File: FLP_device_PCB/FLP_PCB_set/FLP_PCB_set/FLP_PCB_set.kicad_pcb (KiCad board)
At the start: 2 copper layers, 157.8 x 70 mm, 81 parts, among them J3 GRPB052VWVN-RC, J4 OLED, J5 SMA-J-P-X-ST-TH1, Q1 Q_PMOS_DSG, Q2 UMH3N, U1 ESP32-WROOM-32E, U2 TPS61200DRC, U3 MCP73831-2-OT, U4 AMS1117-3.3, U5 CP2104, U6 L86-M33, U7 SX1278, U8 USBLC6-2P6, Y1 32MHz

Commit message: FLP_set add
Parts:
- removed F1: 0603L100SLYR, Resistor_SMD:R_0603_1608Metric
- removed FL1: BLM21PG221SN1D, BLM21PG221SN1D:BEADC2012X105N
- removed R20, R32, R33: 10K, Resistor_SMD:R_0603_1608Metric
- removed R21: 5.1K, Resistor_SMD:R_0402_1005Metric
- removed R30: 22R, Resistor_SMD:R_0402_1005Metric
- removed R31: 1K, Resistor_SMD:R_0603_1608Metric
- removed UART1: 12402012E212A, 12402012E212A:AMPHENOL_12402012E212A
- added BZ1: Buzzer, Buzzer_Beeper:Buzzer_12x9.5RM7.6, F.Cu at (178.4, 110.1)
- added C1: 1uF, Capacitor_SMD:C_0603_1608Metric, F.Cu at (70.7, 155.2)
- added C2: 0.1uF, Capacitor_SMD:C_0603_1608Metric, F.Cu at (66.7, 165.3)
- added C26: 22uF, Capacitor_SMD:C_0805_2012Metric, F.Cu at (172.3, 149.6)
- added C3: PESD0402-140, PESD0402-140:RESC1005X35N, F.Cu at (89.5, 155.0)
- added C36: 0.1uF, Capacitor_SMD:C_0603_1608Metric, F.Cu at (166.1, 104.6)
- added C38: 20pF, Capacitor_SMD:C_0402_1005Metric, F.Cu at (165.5, 124.4)
- added C39: 20pF, Capacitor_SMD:C_0402_1005Metric, F.Cu at (165.5, 126.4)
- added C40: 18pF, Capacitor_SMD:C_0603_1608Metric, F.Cu at (166.1, 109.6)
- added C41: 18pF, Capacitor_SMD:C_0603_1608Metric, F.Cu at (166.1, 112.1)
- added C42: 22uF, Capacitor_SMD:C_0805_2012Metric, F.Cu at (159.0, 142.4)
- added D2: BAT ON, LED_SMD:LED_0805_2012Metric, F.Cu at (94.1, 125.4)
- added D3: TEST, LED_SMD:LED_0805_2012Metric, F.Cu at (94.1, 128.4)
- added D4: USB_ON, LED_SMD:LED_0805_2012Metric, F.Cu at (94.1, 122.4)
- added D5: MBR120VLSFT1G, MBR120VLSFT1G:DIOM3616X98N, F.Cu at (178.1, 151.3)
- added D6: BAT ON, LED_SMD:LED_0805_2012Metric, F.Cu at (176.7, 154.4)
- added D7: USB_ON, LED_SMD:LED_0805_2012Metric, F.Cu at (179.7, 132.9)
- added Find_Host2: SKRPABE010, Diode_SMD:SW_SKRPABE010, F.Cu at (172.0, 105.7)
- added ID1: SKRPABE010, Diode_SMD:SW_SKRPABE010, F.Cu at (172.0, 110.5)
- added J1: GRPB052VWVN-RC, Varistor:SULLINS_GRPB052VWVN-RC, F.Cu at (91.2, 141.6)
- added J10: 61300311121, 61300311121:WURTH_61300311121, F.Cu at (161.9, 152.5)
- added J2: OLED, HTSW-104-20-TM-S:SAMTEC_HTSW-104-20-TM-S, F.Cu at (70.5, 171.0)
- added J6: USB_C_Receptacle_USB2.0_16P, 12402012E212A:AMPHENOL_12402012E212A, F.Cu at (162.4, 137.5)
- added J7: B2B-PH-K-S, B2B_PH_K_S:JST_B2B-PH-K-S, F.Cu at (173.8, 134.4)
- added J8: SMA-J-P-X-ST-TH1, SMA-J-P-X-ST-TH1:SAMTEC_SMA-J-P-X-ST-TH1, F.Cu at (146.4, 135.9)
- added J9: 61300311121, 61300311121:WURTH_61300311121, F.Cu at (161.9, 148.4)
- added L2: 18nH, Capacitor_SMD:C_0402_1005Metric, F.Cu at (92.4, 162.8)
- added L3: 47nH, Capacitor_SMD:C_0402_1005Metric, F.Cu at (140.5, 140.3)
- added R17: 5.1K, Resistor_SMD:R_0402_1005Metric, F.Cu at (96.5, 149.1)
- added R18: 10K, Resistor_SMD:R_0603_1608Metric, F.Cu at (74.7, 162.7)
- added R19: 10K, Resistor_SMD:R_0603_1608Metric, F.Cu at (74.7, 160.2)
- added R24: 2K, Resistor_SMD:R_0402_1005Metric, F.Cu at (176.7, 142.1)
- added R26: 10K, Resistor_SMD:R_0603_1608Metric, F.Cu at (166.1, 114.6)
- added R27: 1M, Resistor_SMD:R_0603_1608Metric, F.Cu at (166.1, 117.2)
- added R28: 10K, Resistor_SMD:R_0603_1608Metric, F.Cu at (166.1, 119.7)
- added S2: SKRPABE010, Diode_SMD:SW_SKRPABE010, F.Cu at (172.0, 115.2)
- added U10: AP2112K-3.3, Package_TO_SOT_SMD:SOT-23-5, F.Cu at (177.1, 147.5)
- added U11: MCP73831-2-OT, Package_TO_SOT_SMD:SOT-23-5, F.Cu at (172.6, 140.5)
- added U12: L86-M33, L86-M33:XCVR_L86-M33, F.Cu at (150.6, 115.4)
- added U13: SX1278, Package_DFN_QFN:QFN-28-1EP_6x6mm_P0.65mm_EP4.8x4.8mm, F.Cu at (146.1, 144.6)
- added U14: CH340N, Package_SO:SOP-8_3.9x4.9mm_P1.27mm, F.Cu at (143.3, 154.1)
- added U9: STM32F103C8T6, STM32F103C8T6:QFP50P900X900X160-48N, F.Cu at (182.1, 122.6)
- added Y2: 32MHz, Crystal:Crystal_SMD_2016-4Pin_2.0x1.6mm, F.Cu at (152.9, 133.2)
- added Y3: ABM3B-8.000MHZ-B2-T, ABM3B-8.000MHZ-B2-T:XTAL_ABM3B-8.000MHZ-B2-T, F.Cu at (171.3, 121.3)
- added Y4: 32.768kHz, Crystal:Crystal_SMD_3215-2Pin_3.2x1.5mm, F.Cu at (170.6, 126.6)
- C10, C9: value 4.7uF -> 22uF; footprint Capacitor_SMD:C_0603_1608Metric -> Capacitor_SMD:C_0805_2012Metric
- C11, C6: value 22uF -> PESD0402-140; footprint Capacitor_SMD:C_0805_2012Metric -> PESD0402-140:RESC1005X35N
- C12, C33: value 22uF -> 0.1uF; footprint Capacitor_SMD:C_0805_2012Metric -> Capacitor_SMD:C_0603_1608Metric
- C13: value PESD0402-140 -> 4.7uF; footprint PESD0402-140:RESC1005X35N -> Capacitor_SMD:C_0603_1608Metric
- C14, C16: value PESD0402-140 -> 22uF; footprint PESD0402-140:RESC1005X35N -> Capacitor_SMD:C_0805_2012Metric
- C17: value PESD0402-140 -> 10uF; footprint PESD0402-140:RESC1005X35N -> Capacitor_SMD:C_0805_2012Metric
- C18, C23, C27: value 0.1uF -> 22uF; footprint Capacitor_SMD:C_0603_1608Metric -> Capacitor_SMD:C_0805_2012Metric
- C19: value 4.7uF -> 12pF; footprint Capacitor_SMD:C_0603_1608Metric -> Capacitor_SMD:C_0402_1005Metric
- C20: value 27pF -> 12pF; footprint Capacitor_SMD:C_0603_1608Metric -> Capacitor_SMD:C_0402_1005Metric
- C21: value 12pF -> 15pF
- C22: value 12pF -> 0.1uF; footprint Capacitor_SMD:C_0402_1005Metric -> Capacitor_SMD:C_0603_1608Metric
- C24: value 22uF -> 3.3pF; footprint Capacitor_SMD:C_0805_2012Metric -> Capacitor_SMD:C_0402_1005Metric
- C28: value 0.1uF -> 1uF
- C30: value 0.1uF -> 12pF; footprint Capacitor_SMD:C_0603_1608Metric -> Capacitor_SMD:C_0402_1005Metric
- C31: value 22uF -> 12pF; footprint Capacitor_SMD:C_0805_2012Metric -> Capacitor_SMD:C_0402_1005Metric
- C32: value 4.7uF -> 15pF; footprint Capacitor_SMD:C_0603_1608Metric -> Capacitor_SMD:C_0402_1005Metric
- C34: value 1uF -> 22uF; footprint Capacitor_SMD:C_0603_1608Metric -> Capacitor_SMD:C_0805_2012Metric
- C35: value 1uF -> 3.3pF; footprint Capacitor_SMD:C_0603_1608Metric -> Capacitor_SMD:C_0402_1005Metric
- C4, C5: value 4.7uF -> PESD0402-140; footprint Capacitor_SMD:C_0603_1608Metric -> PESD0402-140:RESC1005X35N
- C8: value PESD0402-140 -> 1uF; footprint PESD0402-140:RESC1005X35N -> Capacitor_SMD:C_0603_1608Metric
- D1: value MBRA160T3G -> MBR120VLSFT1G; footprint Diode_SMD:DIOM5226X220N -> MBR120VLSFT1G:DIOM3616X98N
- J3: value GRPB052VWVN-RC -> B2B-PH-K-S; footprint Varistor:SULLINS_GRPB052VWVN-RC -> B2B_PH_K_S:JST_B2B-PH-K-S
- J4: value OLED -> USB_C_Receptacle_USB2.0_16P; footprint HTSW-104-20-TM-S:SAMTEC_HTSW-104-20-TM-S -> 12402012E212A:AMPHENOL_12402012E212A
- L1: value 2.2uH -> 47nH; footprint Inductor_SMD:L_1210_3225Metric -> Capacitor_SMD:C_0402_1005Metric
- L4: value 744028000056 -> 18nH; footprint WE-TPC_2811:WE-TPC_2811 -> Capacitor_SMD:C_0402_1005Metric
- Q1: value Q_PMOS_DSG -> DMG3415UQ-7; footprint SI2333DS-T1-E3:SOT95P237X112-3N -> DMG3415UQ-7:SOT96P240X110-3N
- R1: value 2M -> 100R; footprint Resistor_SMD:R_1210_3225Metric -> Resistor_SMD:R_0603_1608Metric
- R10, R29: value 100R -> 10K
- R11: value 100R -> 2.2K
- R12: value 100R -> 100K
- R13: value 100R -> 2K; footprint Resistor_SMD:R_0603_1608Metric -> Resistor_SMD:R_0402_1005Metric
- R14, R15: value 2.2K -> 1K
- R16: value 10K -> 5.1K; footprint Resistor_SMD:R_0603_1608Metric -> Resistor_SMD:R_0402_1005Metric
- R2: value 180K -> 100R; footprint Resistor_SMD:R_1210_3225Metric -> Resistor_SMD:R_0603_1608Metric
- R22: value 10K -> 100K
- R23: value 1K -> 100K
- R25: value 100R -> 1K
- R3, R4: value 10K -> 100R
- R5: value 100R -> 22R
- R6: value 22R -> 10K; footprint Resistor_SMD:R_0402_1005Metric -> Resistor_SMD:R_0603_1608Metric
- R7: value 22R -> 100K; footprint Resistor_SMD:R_0402_1005Metric -> Resistor_SMD:R_0603_1608Metric
- R8: value 5.1K -> 2.2K; footprint Resistor_SMD:R_0402_1005Metric -> Resistor_SMD:R_0603_1608Metric
- U1: value ESP32-WROOM-32E -> L86-M33; footprint RF_Module:ESP32-WROOM-32E -> L86-M33:XCVR_L86-M33
- U2: value TPS61200DRC -> ESP32-WROOM-32E; footprint Package_SON:Texas_S-PVSON-N10_ThermalVias -> RF_Module:ESP32-WROOM-32E
- U3: value MCP73831-2-OT -> AP2112K-3.3; footprint Package_TO_SOT_SMD:SOT95P280X145-5N -> Package_TO_SOT_SMD:SOT-23-5
- U4: value AMS1117-3.3 -> CP2104; footprint Package_TO_SOT_SMD:SOT-223-3_TabPin2 -> Package_DFN_QFN:QFN-24-1EP_4x4mm_P0.5mm_EP2.6x2.6mm
- U5: value CP2104 -> MCP73831-2-OT; footprint Package_DFN_QFN:QFN-24-1EP_4x4mm_P0.5mm_EP2.6x2.6mm -> Package_TO_SOT_SMD:SOT-23-5
- U6: value L86-M33 -> USBLC6-2P6; footprint L86-M33:XCVR_L86-M33 -> Package_TO_SOT_SMD:SOT-666
- moved U1 108.7 mm to (48.7, 166.0)
- moved U8 107.7 mm to (163.3, 142.7), turned to 0 degrees
- moved C37 77.0 mm to (166.1, 107.1)
- moved C27 75.5 mm to (177.4, 139.6)
- moved U2 74.3 mm to (61.9, 139.9)
- moved C25 71.0 mm to (172.3, 146.6)
- moved L4 67.7 mm to (140.5, 142.2)
- moved R25 67.4 mm to (179.5, 135.7)
- moved R29 64.3 mm to (166.1, 122.2)
- moved U5 63.8 mm to (89.3, 123.2), turned to 0 degrees
- moved J4 61.0 mm to (92.3, 117.5)
- moved C34 55.7 mm to (152.4, 142.0)
- moved R22 55.0 mm to (172.1, 152.4)
- moved R23 55.0 mm to (172.1, 154.9)
- moved C28 54.2 mm to (145.5, 127.7)
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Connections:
- C10 pad 1: Net-(U5-VPP) -> /FLP_host/3.3V_OUT
- C11 pad 1: /FLP_host/5v_OUT -> /FLP_host/I2C_SCL
- C13 pad 1: Net-(C13-Pad1) -> /FLP_host/3.3V_OUT
- C14 pad 1: Net-(C14-Pad1) -> Net-(D2-A)
- C15 pad 1: Net-(C15-Pad1) -> /FLP_host/I2C_SDL
- C16 pad 1: /FLP_host/I2C_SCL -> /FLP_host/3.3V_OUT
- C17 pad 1: /FLP_host/I2C_SDL -> /FLP_host/3.3V_OUT
- C18 pad 1: /FLP_host/3.3V_OUT -> /FLP_host/VBAT
- C19 pad 1: /FLP_host/3.3V_OUT -> GND
- C19 pad 2: GND -> Net-(U7-XTA)
- C20 pad 1: Net-(C20-Pad1) -> GND
- C20 pad 2: Net-(C20-Pad2) -> Net-(U7-XTB)
- C21 pad 1: GND -> Net-(C21-Pad1)
- C21 pad 2: Net-(U7-XTB) -> Net-(C21-Pad2)
- C22 pad 1: GND -> /FLP_host/3.3V_OUT
- C22 pad 2: Net-(U7-XTA) -> GND
- C23 pad 1: /FLP_host/3.3V_OUT -> GND
- C23 pad 2: GND -> /FLP_host/3.3V_OUT
- C24 pad 1: GND -> Net-(U7-PA_BOOST)
- C24 pad 2: /FLP_host/3.3V_OUT -> GND
- C25 pad 1: /FLP_host/3.3V_OUT -> Net-(D6-A)
- C27 pad 1: GND -> /FLP_terminal/Bat/VBAT
- C27 pad 2: Net-(C27-Pad2) -> GND
- C28 pad 1: GND -> /FLP_terminal/BOOT_Mode/3.3V_in
- C28 pad 2: Net-(U5-REGIN) -> GND
- C29 pad 1: Net-(U5-REGIN) -> /FLP_terminal/BOOT_Mode/3.3V_in
- C30 pad 1: /FLP_host/3.3V_OUT -> GND
- C30 pad 2: GND -> Net-(U13-XTA)
- C31 pad 2: /FLP_host/3.3V_OUT -> Net-(U13-XTB)
- C32 pad 1: Net-(Q1-D) -> Net-(C32-Pad1)
- C32 pad 2: GND -> Net-(C32-Pad2)
- C33 pad 1: /FLP_host/5v_OUT -> /FLP_terminal/BOOT_Mode/3.3V_in
- C34 pad 1: Net-(U2-VAUX) -> GND
- C34 pad 2: GND -> /FLP_terminal/BOOT_Mode/3.3V_in
- C35 pad 1: /FLP_host/3.3V_OUT -> Net-(U13-PA_BOOST)
- C37 pad 1: EN -> /FLP_terminal/STM32/Buzzer
- C4 pad 1: /FLP_host/BAT_input -> GND
- C4 pad 2: GND -> Net-(C4-Pad2)
- C5 pad 1: Net-(BT1-+) -> GND
- C5 pad 2: GND -> Net-(C5-Pad2)
- C6 pad 1: /FLP_host/3.3V_OUT -> Net-(C6-Pad1)
- C8 pad 1: Net-(C8-Pad1) -> /FLP_host/3.3V_OUT
- C9 pad 1: Net-(U5-REGIN) -> /FLP_host/3.3V_OUT
- Ctrl1 pad 3: Net-(Ctrl1-Pad3) -> /FLP_host/Ctrl
- Ctrl1 pad 4: Net-(Ctrl1-Pad3) -> /FLP_host/Ctrl
- Find_Host1 pad 3: Net-(Find_Host1-Pad3) -> /FLP_host/Find_Host
- Find_Host1 pad 4: Net-(Find_Host1-Pad3) -> /FLP_host/Find_Host
- J3 pad 1: /FLP_host/3.3V_OUT -> /FLP_host/VBAT
- J3 pad 2: Net-(C8-Pad1) -> GND
- J5 pad 1: Net-(C20-Pad1) -> Net-(C21-Pad2)
- L1 pad 1: Net-(Q1-D) -> GND
- L1 pad 2: Net-(U2-L) -> Net-(C21-Pad1)
- L4 pad 1: Net-(C20-Pad2) -> Net-(C32-Pad1)
- L4 pad 2: Net-(U7-PA_BOOST) -> Net-(U13-PA_BOOST)
- Q1 pad 1: Net-(Q1-D) -> /FLP_host/5v_USB_OUT
- Q1 pad 2: Net-(BT1-+) -> Net-(D2-A)
- Q1 pad 3: Net-(Q1-G) -> /FLP_host/VBAT
- R1 pad 1: Net-(Q1-D) -> /FLP_host/MTDI
- R1 pad 2: Net-(U2-UVLO) -> Net-(C6-Pad1)
- R10 pad 1: /FLP_host/MTDI -> /FLP_host/DTR
- R10 pad 2: Net-(C15-Pad1) -> Net-(Q2B-B2)
- R11 pad 1: /FLP_host/MTDO -> /FLP_host/I2C_SDL
- R11 pad 2: Net-(C14-Pad1) -> /FLP_host/3.3V_OUT
- R12 pad 1: /FLP_host/MTCK -> Net-(U3-EN)
- R12 pad 2: Net-(C13-Pad1) -> Net-(D2-A)
- R13 pad 1: /FLP_host/MTMS -> GND
- R13 pad 2: Net-(C8-Pad1) -> Net-(U5-PROG)
- R14 pad 1: /FLP_host/I2C_SCL -> Net-(D3-K)
- R14 pad 2: /FLP_host/3.3V_OUT -> GND
- R15 pad 1: /FLP_host/I2C_SDL -> Net-(U5-STAT)
- R15 pad 2: /FLP_host/3.3V_OUT -> Net-(D4-K)
- R16 pad 1: Net-(Find_Host1-Pad3) -> GND
- R16 pad 2: GND -> Net-(J4-CC2)
- R2 pad 1: Net-(U2-UVLO) -> /FLP_host/MTDO
- R2 pad 2: GND -> Net-(C5-Pad2)
- R22 pad 1: Net-(U5-~{RST}) -> /FLP_terminal/Bat/5v_USB_OUT
- R22 pad 2: /FLP_host/3.3V_OUT -> GND
- R23 pad 1: /FLP_host/BAT_input -> Net-(U10-EN)
- R23 pad 2: Net-(Q1-G) -> Net-(D6-A)
- R25 pad 1: Net-(Find_Host1-Pad3) -> Net-(U11-STAT)
- R25 pad 2: /FLP_host/Find_Host -> Net-(D7-K)
- R29 pad 1: Net-(Ctrl1-Pad3) -> /FLP_terminal/STM32/Find_Host
- R29 pad 2: /FLP_host/Ctrl -> GND
- R3 pad 1: Net-(U3-PROG) -> /FLP_host/MTCK
- R3 pad 2: GND -> Net-(C4-Pad2)
- R4 pad 1: /FLP_host/BAT_input -> /FLP_host/MTMS
- R4 pad 2: GND -> Net-(C3-Pad1)
- R5 pad 1: /FLP_host/GPS_Reset -> Net-(C2-Pad2)
- R5 pad 2: Net-(U6-~{RESET}) -> EN
- R6 pad 1: /FLP_host/TX -> EN
- R6 pad 2: Net-(U5-RXD) -> /FLP_host/3.3V_OUT
- R7 pad 1: /FLP_host/RX -> /FLP_host/5v_USB_OUT
- R7 pad 2: Net-(U5-TXD) -> GND
- R8 pad 1: GND -> /FLP_host/I2C_SCL
- R8 pad 2: Net-(UART1-CC2) -> /FLP_host/3.3V_OUT
- R9 pad 1: EN -> /FLP_host/RTS
- R9 pad 2: /FLP_host/3.3V_OUT -> Net-(Q2A-B1)
- S1 pad 3: Net-(C27-Pad2) -> Net-(C2-Pad2)
- S1 pad 4: Net-(C27-Pad2) -> Net-(C2-Pad2)
- U1 pad 1: GND -> /FLP_host/GPS_Rx
- U1 pad 10: /FLP_host/Find_Host -> /FLP_host/GPS_Reset
- U1 pad 11: /FLP_host/DIO0(IRQ) -> unconnected-(U1-EX_ANT-Pad11)
- U1 pad 12: unconnected-(U1-IO27-Pad12) -> GND
- U1 pad 2: /FLP_host/3.3V_OUT -> /FLP_host/GPS_TX
- U1 pad 3: EN -> GND
- U1 pad 4: unconnected-(U1-SENSOR_VP-Pad4) -> /FLP_host/3.3V_OUT
- U1 pad 5: unconnected-(U1-SENSOR_VN-Pad5) -> /FLP_host/3.3V_OUT
- U1 pad 8: /FLP_host/GPS_TX -> unconnected-(U1-AADET_N-Pad8)
- U1 pad 9: /FLP_host/GPS_Rx -> (no net)
- U2 pad 1: Net-(U2-VAUX) -> GND
- U2 pad 10: /FLP_host/5v_OUT -> /FLP_host/Find_Host
- U2 pad 11: GND -> /FLP_host/DIO0(IRQ)
- U2 pad 2: /FLP_host/5v_OUT -> /FLP_host/3.3V_OUT
- U2 pad 3: Net-(U2-L) -> EN
- U2 pad 4: GND -> unconnected-(U2-SENSOR_VP-Pad4)
- U2 pad 5: Net-(Q1-D) -> unconnected-(U2-SENSOR_VN-Pad5)
- U2 pad 6: Net-(Q1-D) -> unconnected-(U2-IO34-Pad6)
- U2 pad 7: Net-(U2-UVLO) -> /FLP_host/TEST LED
- U2 pad 8: Net-(Q1-D) -> /FLP_host/GPS_TX
- U2 pad 9: GND -> /FLP_host/GPS_Rx
- U3 pad 1: unconnected-(U3-STAT-Pad1) -> Net-(D2-A)
- U3 pad 3: Net-(BT1-+) -> Net-(U3-EN)
- U3 pad 4: /FLP_host/BAT_input -> unconnected-(U3-NC-Pad4)
- U3 pad 5: Net-(U3-PROG) -> /FLP_host/3.3V_OUT
- U4 pad 1: GND -> unconnected-(U4-~{RI}-Pad1)
- U4 pad 2: /FLP_host/3.3V_OUT -> GND
- U4 pad 3: /FLP_host/5v_OUT -> Net-(U4-D+)
- U5 pad 1: unconnected-(U5-~{RI}-Pad1) -> Net-(U5-STAT)
- U5 pad 3: Net-(U5-D+) -> /FLP_host/VBAT
- U5 pad 4: Net-(U5-D-) -> /FLP_host/5v_USB_OUT
- U5 pad 5: /FLP_host/3.3V_OUT -> Net-(U5-PROG)
- U6 pad 1: /FLP_host/GPS_Rx -> Net-(J4-D--PadA7)
- U6 pad 2: /FLP_host/GPS_TX -> /FLP_host/3.3V_OUT
- U6 pad 3: GND -> Net-(J4-D+-PadA6)
- U6 pad 4: /FLP_host/3.3V_OUT -> Net-(U4-D+)
- U6 pad 5: /FLP_host/3.3V_OUT -> GND
- U6 pad 6: unconnected-(U6-1PPS-Pad6) -> Net-(U4-D-)
- U8 pad 4: Net-(U5-D-) -> /FLP_terminal/UART_USB/D-
- U8 pad 5: Net-(U5-REGIN) -> /FLP_terminal/BOOT_Mode/3.3V_in
- U8 pad 6: Net-(U5-D+) -> /FLP_terminal/UART_USB/D+
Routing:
- net Net-(U5-D+): track 5.51 -> 0.00 mm
- net Net-(U5-D-): track 5.28 -> 0.00 mm
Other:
- board size 157.8 x 70 mm -> 152.1 x 70.1 mm

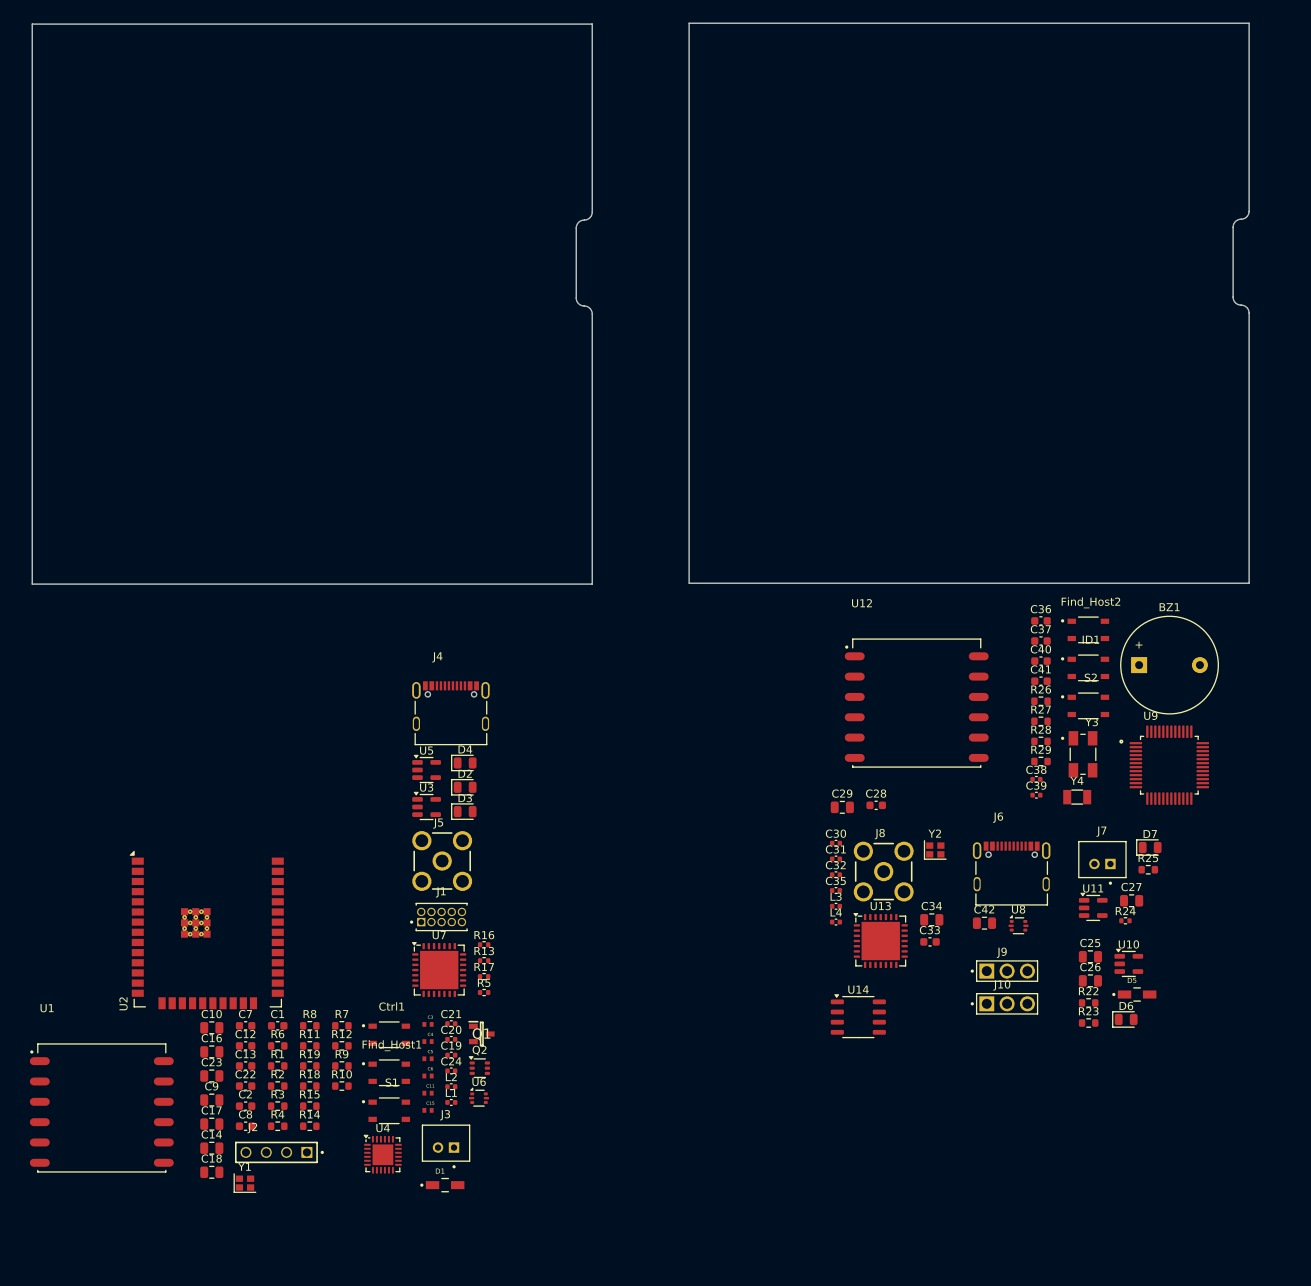
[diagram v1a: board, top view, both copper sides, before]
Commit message: PCB fixing end adding description pdf
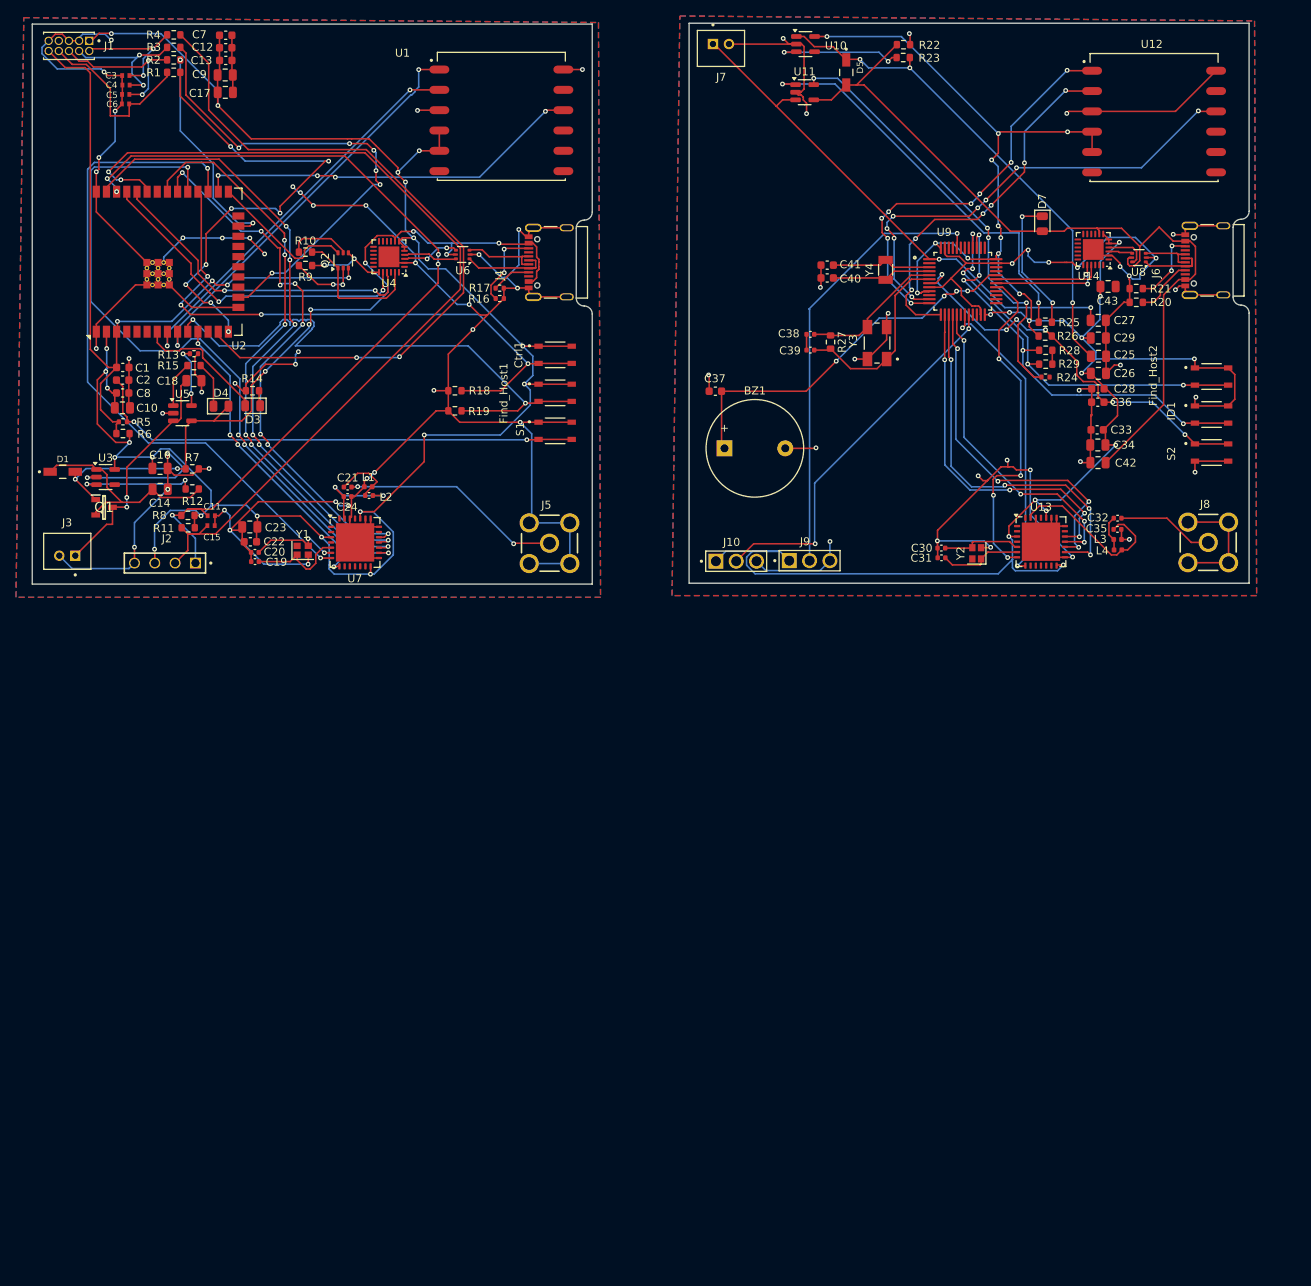
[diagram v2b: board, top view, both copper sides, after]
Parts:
- removed D2, D6: BAT ON, LED_SMD:LED_0805_2012Metric
- added C43: 10uF, Capacitor_SMD:C_0805_2012Metric, F.Cu at (174.5, 62.8)
- added R20: 5.1K, Resistor_SMD:R_0603_1608Metric, F.Cu at (178.0, 64.8)
- added R21: 5.1K, Resistor_SMD:R_0603_1608Metric, F.Cu at (178.0, 63.1)
- BZ1: value Buzzer -> FQ 010
- D3: value TEST -> 150080GS75000
- D4, D7: value USB_ON -> 150080GS75000
- J4, J6: value USB_C_Receptacle_USB2.0_16P -> 12402012E212A
- L1, L3, L4: footprint Capacitor_SMD:C_0402_1005Metric -> Inductor_SMD:L_0402_1005Metric
- U14: value CH340N -> CP2104; footprint Package_SO:SOP-8_3.9x4.9mm_P1.27mm -> Package_DFN_QFN:QFN-24-1EP_4x4mm_P0.5mm_EP2.6x2.6mm
- moved R4 137.0 mm to (57.7, 31.3), turned to 180 degrees
- moved U1 133.6 mm to (98.6, 42.0)
- moved R3 133.0 mm to (57.7, 32.9), turned to 180 degrees
- moved C17 129.0 mm to (64.1, 38.5)
- moved R2 128.9 mm to (57.7, 34.5), turned to 180 degrees
- moved C9 128.1 mm to (64.1, 36.4)
- moved C6 127.3 mm to (51.7, 40.0), turned to 180 degrees
- moved C5 126.3 mm to (51.7, 38.8)
- moved C13 125.7 mm to (64.2, 34.5)
- moved C4 125.4 mm to (51.7, 37.6)
- moved R1 124.9 mm to (57.7, 36.0), turned to 180 degrees
- moved C12 124.8 mm to (64.2, 33.0)
- moved C3 124.5 mm to (51.7, 36.4), turned to 180 degrees
- moved C7 123.8 mm to (64.2, 31.4)
- moved R23 122.9 mm to (148.9, 34.2)
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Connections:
- Find_Host2 pad 1: /FLP_terminal/STM32/3.3V_OUT -> /FLP_terminal/BOOT_Mode/3.3V_in
- Find_Host2 pad 2: /FLP_terminal/STM32/3.3V_OUT -> /FLP_terminal/BOOT_Mode/3.3V_in
- ID1 pad 1: /FLP_terminal/STM32/3.3V_OUT -> /FLP_terminal/BOOT_Mode/3.3V_in
- ID1 pad 2: /FLP_terminal/STM32/3.3V_OUT -> /FLP_terminal/BOOT_Mode/3.3V_in
- U14 pad 1: /FLP_terminal/UART_USB/D+ -> unconnected-(U14-~{RI}-Pad1)
- U14 pad 2: /FLP_terminal/UART_USB/D- -> GND
- U14 pad 3: GND -> /FLP_terminal/UART_USB/D+
- U14 pad 4: unconnected-(U14-~{RTS}-Pad4) -> /FLP_terminal/UART_USB/D-
- U14 pad 5: /FLP_terminal/Bat/5v_USB_OUT -> /FLP_terminal/BOOT_Mode/3.3V_in
- U14 pad 6: /FLP_terminal/STM32/TX -> /FLP_terminal/BOOT_Mode/3.3V_in
- U14 pad 7: /FLP_terminal/STM32/RX -> /FLP_terminal/BOOT_Mode/3.3V_in
- U14 pad 8: GND -> /FLP_terminal/Bat/5v_USB_OUT
- U6 pad 2: /FLP_host/3.3V_OUT -> GND
- U6 pad 5: GND -> /FLP_host/5v_USB_OUT
- U8 pad 1: Net-(J6-D+-PadA6) -> Net-(J6-D--PadA7)
- U8 pad 3: Net-(J6-D--PadA7) -> Net-(J6-D+-PadA6)
- U8 pad 4: /FLP_terminal/UART_USB/D- -> /FLP_terminal/UART_USB/D+
- U8 pad 5: /FLP_terminal/BOOT_Mode/3.3V_in -> /FLP_terminal/Bat/5v_USB_OUT
- U8 pad 6: /FLP_terminal/UART_USB/D+ -> /FLP_terminal/UART_USB/D-
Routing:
- net GND: track 0.00 -> 635.3 mm, vias 0 -> 72
- net /FLP_terminal/BOOT_Mode/3.3V_in: track 0.00 -> 255.4 mm, vias 0 -> 25
- net /FLP_host/3.3V_OUT: track 0.00 -> 253.3 mm, vias 0 -> 21
- net /FLP_host/I2C_SDL: track 0.00 -> 116.2 mm, vias 0 -> 2
- net /FLP_host/I2C_SCL: track 0.00 -> 109.0 mm, vias 0 -> 5
- net /FLP_terminal/Bat/5v_USB_OUT: track 0.00 -> 104.4 mm
- net /FLP_host/5v_USB_OUT: track 0.00 -> 100.8 mm, vias 0 -> 9
- net EN: track 0.00 -> 94.4 mm, vias 0 -> 4
- net /FLP_host/MTMS: track 0.00 -> 91.2 mm, vias 0 -> 2
- net /FLP_host/SCK: track 0.00 -> 89.0 mm, vias 0 -> 4
- net /FLP_host/RESET: track 0.00 -> 84.8 mm, vias 0 -> 2
- net /FLP_host/MOSI: track 0.00 -> 80.6 mm, vias 0 -> 6
- net /FLP_host/Ctrl: track 0.00 -> 77.7 mm, vias 0 -> 4
- net /FLP_host/MISO: track 0.00 -> 73.0 mm, vias 0 -> 6
- net /FLP_host/Find_Host: track 0.00 -> 71.1 mm, vias 0 -> 2
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- added copper zone on B.Cu, net GND
- added copper zone on F.Cu, net GND
